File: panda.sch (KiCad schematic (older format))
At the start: 26 parts, among them J1 USB, J2 ICSP, U1 ATMEGA328-P, U2 MAX7219, Y1 Crystal_Small

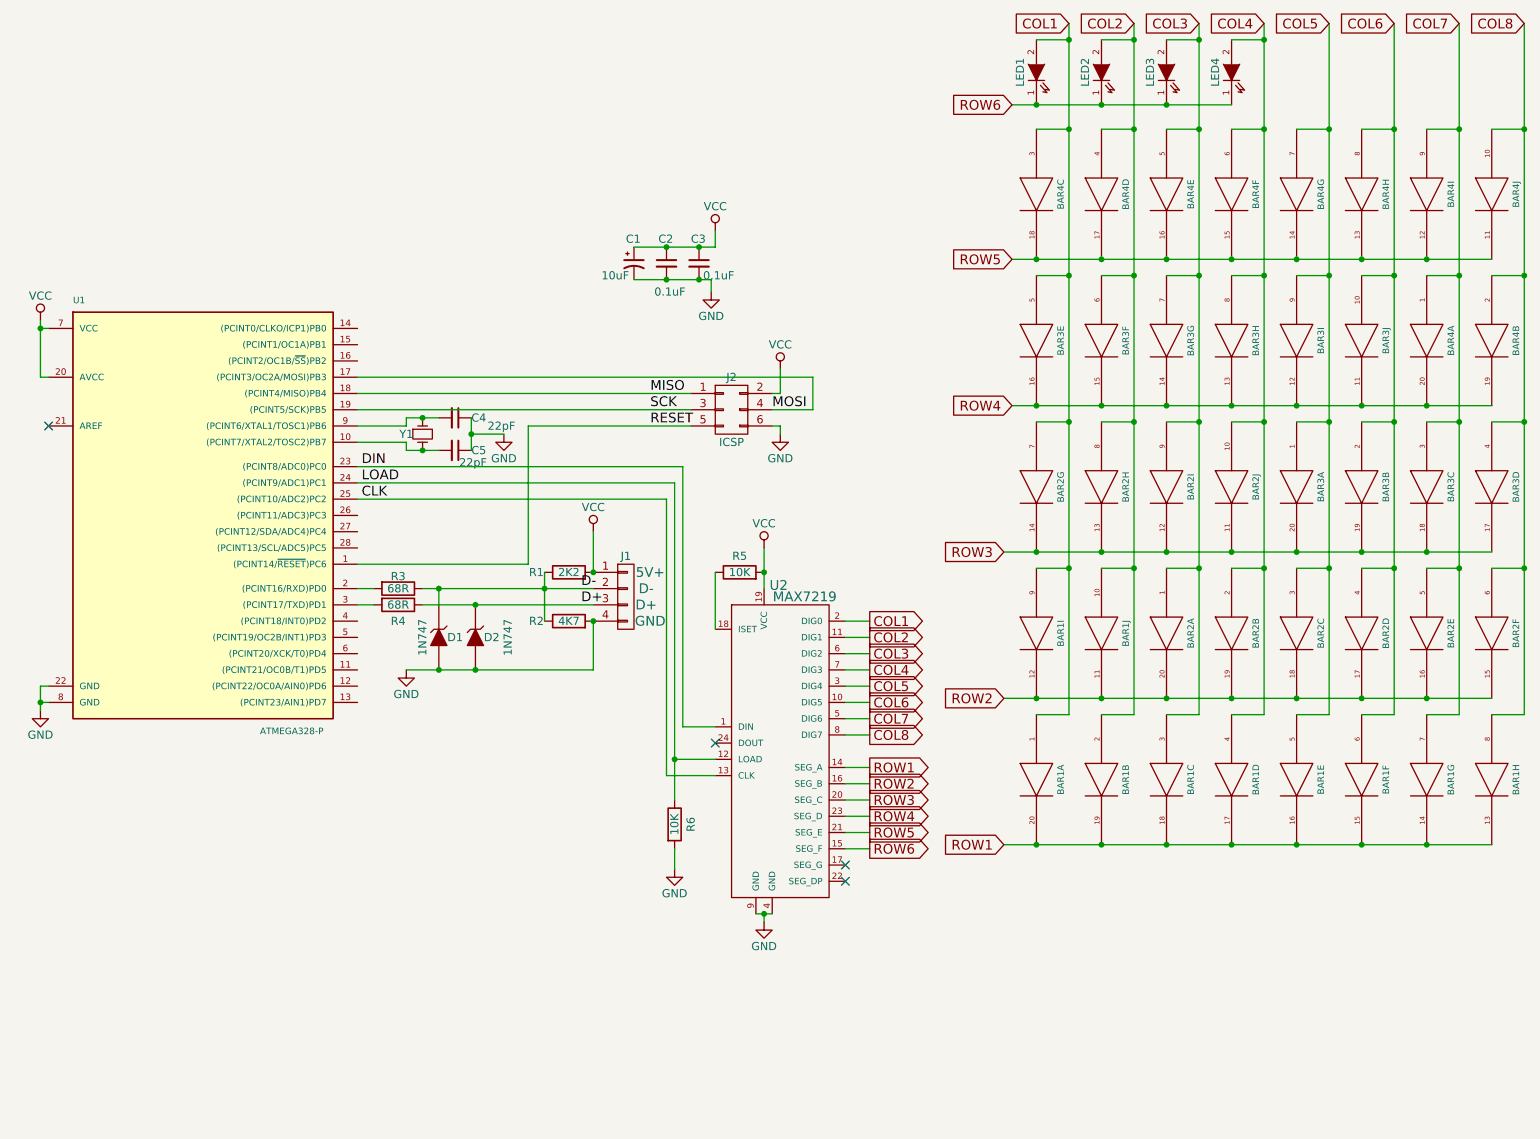
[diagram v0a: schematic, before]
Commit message: Move chips and polarized capacitor to other side.  Makes for easier socketing.
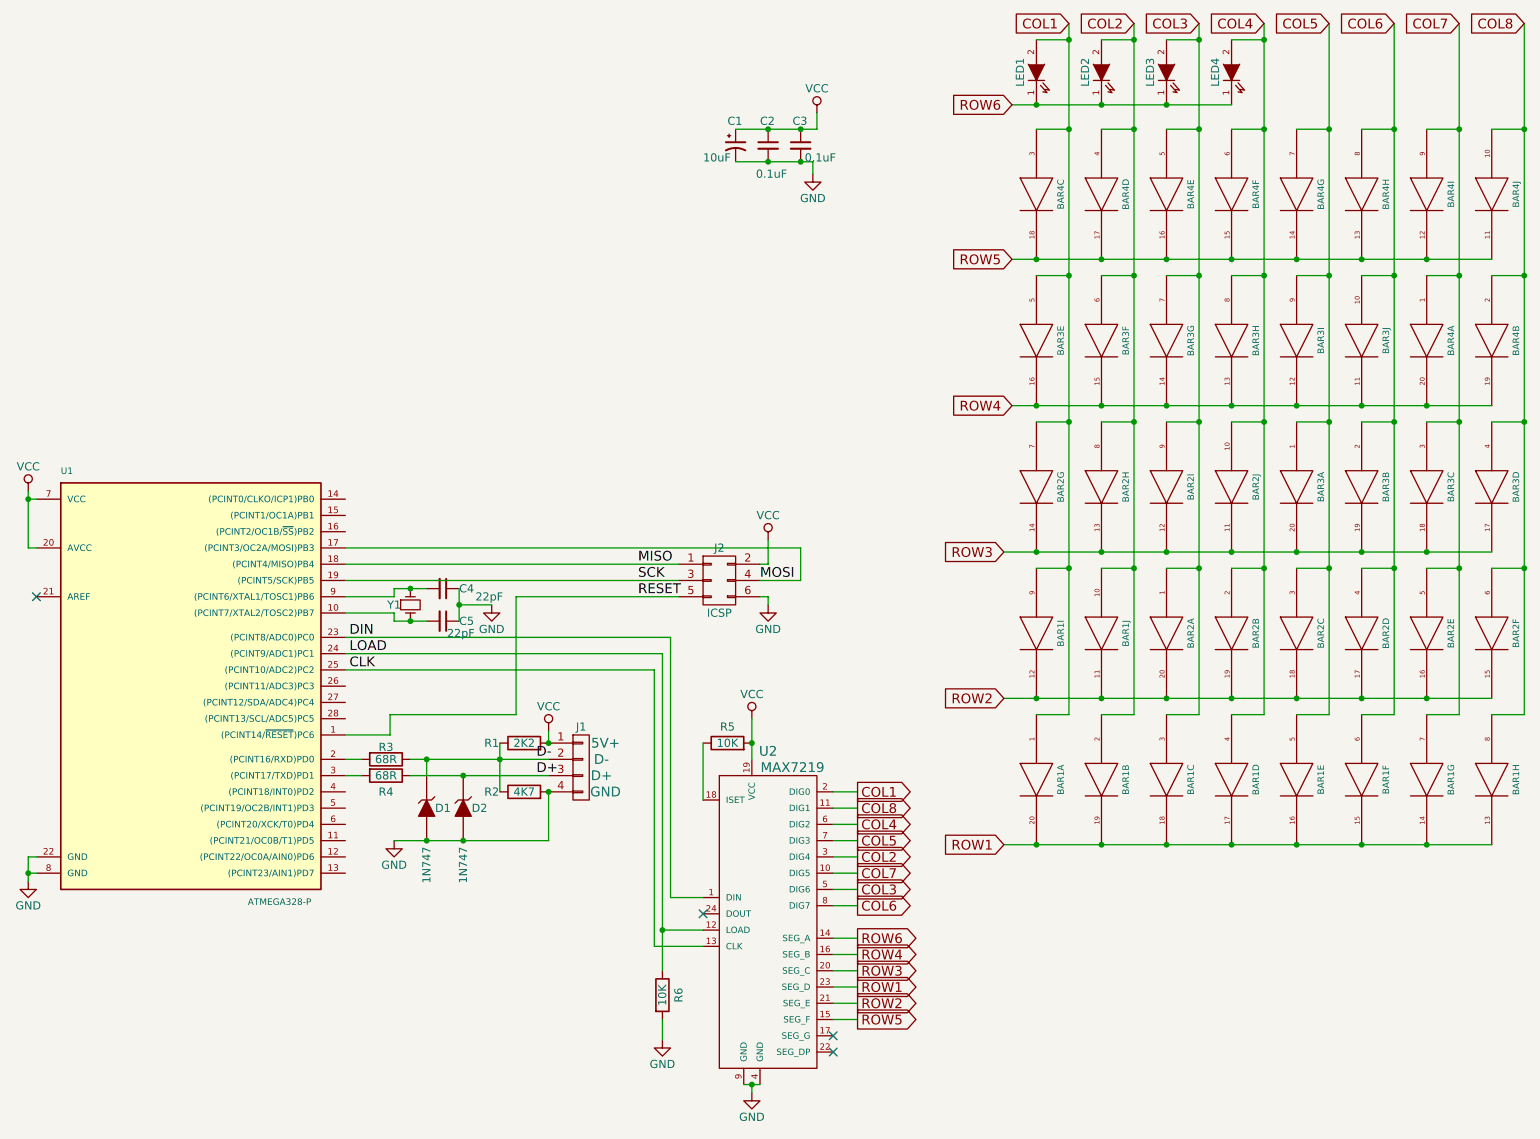
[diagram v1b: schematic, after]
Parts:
- Y1: value Crystal_Small -> 12MHz; footprint Crystals:Crystal_HC48-U_Vertical -> Crystals:Crystal_HC49-U_Vertical
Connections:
- net COL2: now also U2.3 (DIG4); no longer U2.11 (DIG1)
- net COL3: now also U2.5 (DIG6); no longer U2.6 (DIG2)
- net COL4: now also U2.6 (DIG2); no longer U2.7 (DIG3)
- net COL5: now also U2.7 (DIG3); no longer U2.3 (DIG4)
- net COL6: now also U2.8 (DIG7); no longer U2.10 (DIG5)
- net COL7: now also U2.10 (DIG5); no longer U2.5 (DIG6)
- net COL8: now also U2.11 (DIG1); no longer U2.8 (DIG7)
- net ROW1: now also U2.23 (SEG_D); no longer U2.14 (SEG_A)
- net ROW2: now also U2.21 (SEG_E); no longer U2.16 (SEG_B)
- net ROW4: now also U2.16 (SEG_B); no longer U2.23 (SEG_D)
- net ROW5: now also U2.15 (SEG_F); no longer U2.21 (SEG_E)
- net ROW6: now also U2.14 (SEG_A); no longer U2.15 (SEG_F)
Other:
- moved on the sheet: C1, C2, C3, C4, C5, D1, D2, J1, J2, R1, R2, R3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

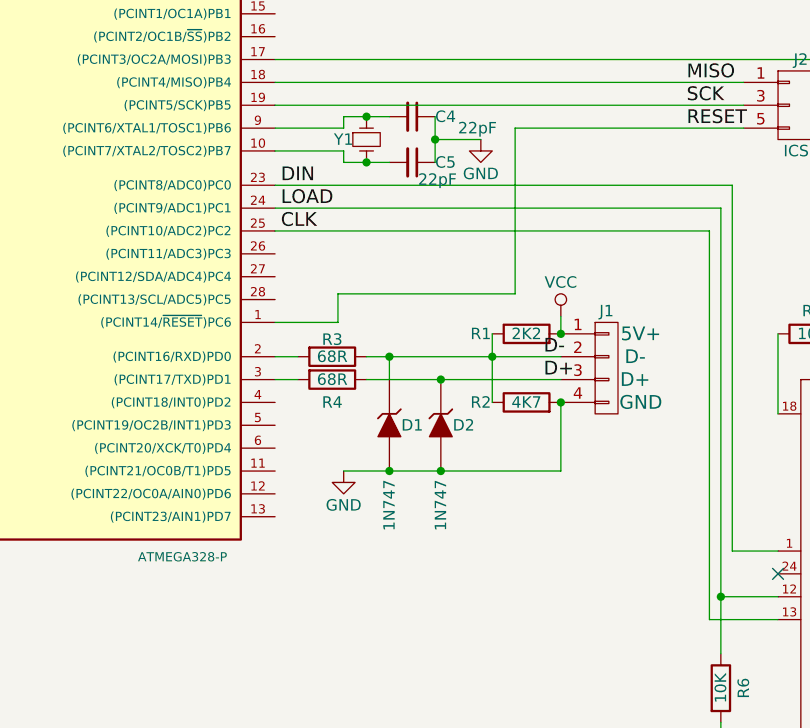
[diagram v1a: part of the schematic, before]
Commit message: Add voltage labels to zener diodes.
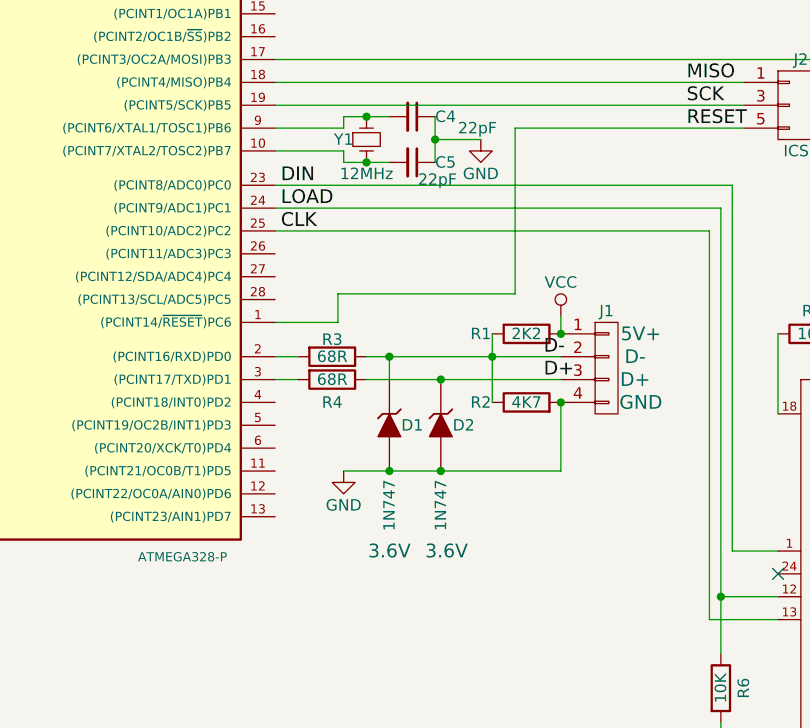
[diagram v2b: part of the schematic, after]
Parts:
- D1, D2: Voltage (none) -> 3.6V
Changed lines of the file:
@@
 F 2 "Diodes_ThroughHole:Diode_DO-35_SOD27_Horizontal_RM10" H 3250 6000 60  0001 C CNN
 F 3 "" H 3250 6000 60  0000 C CNN
+F 4 "3.6V" V 3800 6000 60  0000 C CNN "Voltage"
 	1    3250 6000
 	0    1    1    0
@@
 F 2 "Diodes_ThroughHole:Diode_DO-35_SOD27_Horizontal_RM10" H 3475 6000 60  0001 C CNN
 F 3 "" H 3475 6000 60  0000 C CNN
+F 4 "3.6V" V 4025 6025 60  0000 C CNN "Voltage"
 	1    3475 6000
 	0    1    1    0
@@
 P 3150 4750
 F 0 "Y1" V 3150 4650 50  0000 C CNN
-F 1 "12MHz" H 3150 4650 50  0001 C CNN
+F 1 "12MHz" V 3300 4750 50  0000 C CNN
 F 2 "Crystals:Crystal_HC49-U_Vertical" H 3150 4750 60  0001 C CNN
 F 3 "" H 3150 4750 60  0000 C CNN

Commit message: Cleanup and wording.
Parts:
- LED1, LED2, LED3, LED4: footprint LEDs:LED-5MM -> MyLEDs:LED-5MM
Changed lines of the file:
@@
 F 0 "LED1" H 7000 1575 50  0000 C CNN
 F 1 "LED" H 7000 1375 50  0001 C CNN
-F 2 "LEDs:LED-5MM" H 7000 1475 60  0001 C CNN
+F 2 "MyLEDs:LED-5MM" H 7000 1475 60  0001 C CNN
 F 3 "" H 7000 1475 60  0000 C CNN
 	1    7000 1475
@@
 F 0 "LED2" H 7400 1575 50  0000 C CNN
 F 1 "LED" H 7400 1375 50  0001 C CNN
-F 2 "LEDs:LED-5MM" H 7400 1475 60  0001 C CNN
+F 2 "MyLEDs:LED-5MM" H 7400 1475 60  0001 C CNN
 F 3 "" H 7400 1475 60  0000 C CNN
 	1    7400 1475
@@
 F 0 "LED3" H 7800 1575 50  0000 C CNN
 F 1 "LED" H 7800 1375 50  0001 C CNN
-F 2 "LEDs:LED-5MM" H 7800 1475 60  0001 C CNN
+F 2 "MyLEDs:LED-5MM" H 7800 1475 60  0001 C CNN
 F 3 "" H 7800 1475 60  0000 C CNN
 	1    7800 1475
@@
 F 0 "LED4" H 8200 1575 50  0000 C CNN
 F 1 "LED" H 8200 1375 50  0001 C CNN
-F 2 "LEDs:LED-5MM" H 8200 1475 60  0001 C CNN
+F 2 "MyLEDs:LED-5MM" H 8200 1475 60  0001 C CNN
 F 3 "" H 8200 1475 60  0000 C CNN
 	1    8200 1475
